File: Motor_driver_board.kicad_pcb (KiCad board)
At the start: 4 copper layers, 90 x 90 mm, 93 parts, among them J1 USB_B_Micro, J2 Screw_Terminal_01x02, J3 Screw_Terminal_01x02, J4 Screw_Terminal_01x03, SW1 Boot, SW2 Reset, U1 LM2596DSADJG, U10 NTMFS5C628NLT1G, U11 NTMFS5C628NLT1G, U12 NTMFS5C628NLT1G, U13 LM393, U2 TPS62A01ADRL, U3 ESP32-S3-MINI-1, U4 USBLC6-2SC6, U5 DRV8323RSRGZR, U6 NTMFS5C628NLT1G, U7 NTMFS5C628NLT1G, U8 NTMFS5C628NLT1G, U9 NTMFS5C628NLT1G

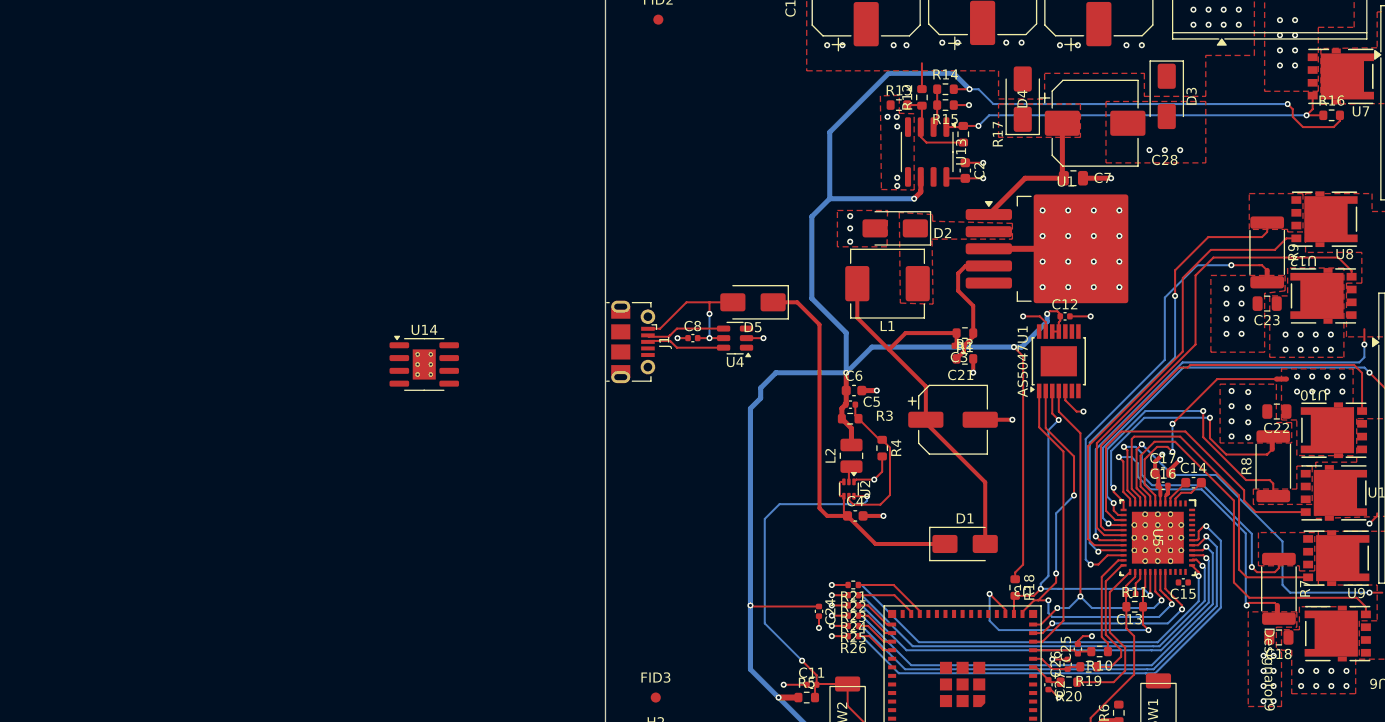
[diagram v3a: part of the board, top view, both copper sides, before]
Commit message: changed regulators, added resistor for slew rate on braking mosfet
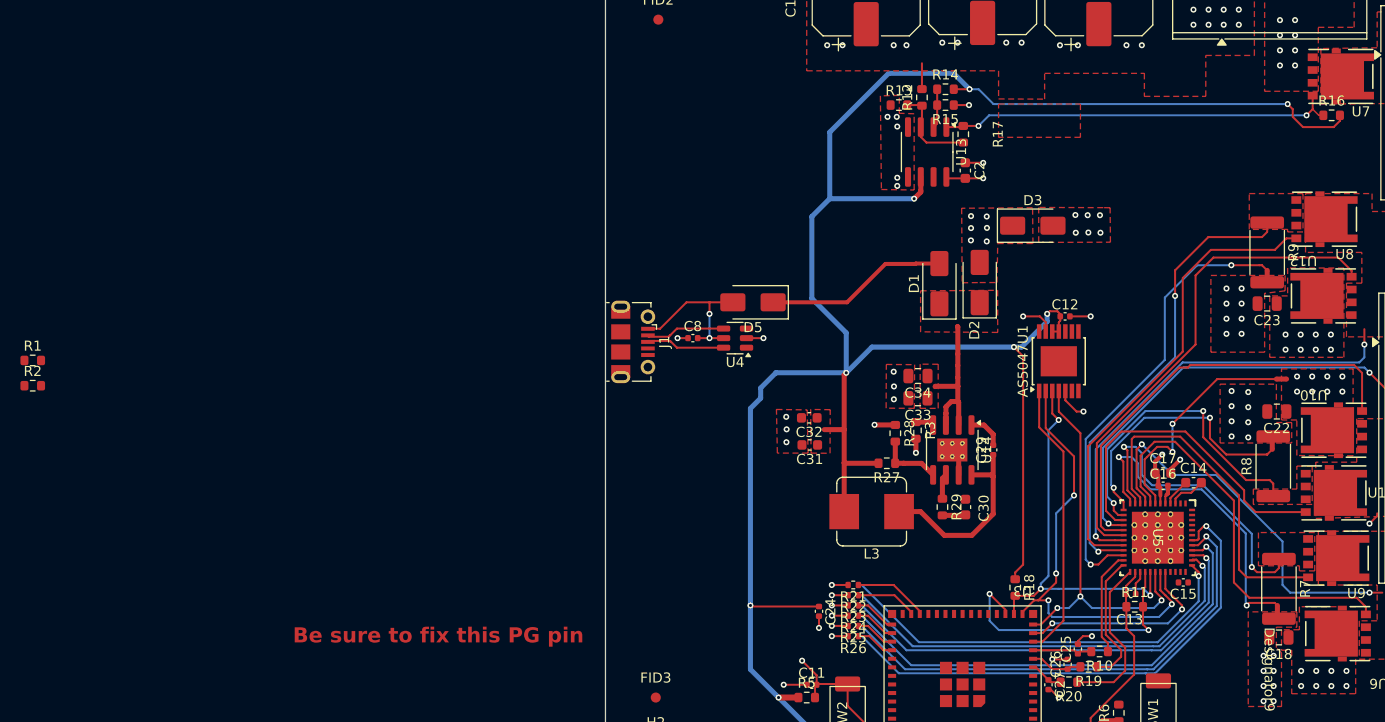
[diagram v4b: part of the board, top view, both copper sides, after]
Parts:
- removed C21: 220 uF, Capacitor_SMD:CP_Elec_6.3x7.7
- removed C28: 100 uF, Capacitor_SMD:CP_Elec_8x10
- removed C3: 15 nF, Capacitor_SMD:C_0402_1005Metric
- removed C4: 4.7 uF, Capacitor_SMD:C_0603_1608Metric
- removed C5: 10 pF, Capacitor_SMD:C_0402_1005Metric
- removed C6: 22 uF, Capacitor_SMD:C_0603_1608Metric
- removed C7: 4.7 uF, Capacitor_SMD:C_0805_2012Metric
- removed D4: SS34, Diode_SMD:D_SMA
- removed L1: 33 uH, Inductor_SMD:L_TechFuse_SL0630
- removed L2: 1.0 uH, Inductor_SMD:L_1008_2520Metric
- removed R4: 100k, Resistor_SMD:R_0603_1608Metric
- removed U1: LM2596DSADJG, Package_TO_SOT_SMD:TO-263-5_TabPin6
- removed U2: TPS62A01ADRL, Package_TO_SOT_SMD:SOT-563
- added C29: 0.1 uF, Capacitor_SMD:C_0402_1005Metric, F.Cu at (167.4, 101.9)
- added C30: 5.6 nF, Capacitor_SMD:C_0603_1608Metric, F.Cu at (164.6, 107.6)
- added C31: 22 uF, Capacitor_SMD:C_0603_1608Metric, F.Cu at (149.2, 101.4)
- added C32: 22 uF, Capacitor_SMD:C_0603_1608Metric, F.Cu at (149.1, 98.7)
- added C33: 10 uF, Capacitor_SMD:C_0805_2012Metric, F.Cu at (159.9, 96.8)
- added C34: 10 uF, Capacitor_SMD:C_0805_2012Metric, F.Cu at (159.9, 94.6)
- added L3: 6.8 uH, Inductor_SMD:L_Bourns_SRP7028A_7.3x6.6mm, F.Cu at (155.3, 108.0)
- added R27: 31.6k, Resistor_SMD:R_0603_1608Metric, F.Cu at (156.8, 103.2)
- added R28: 10k, Resistor_SMD:R_0603_1608Metric, F.Cu at (157.6, 100.2)
- added R29: 9.31k, Resistor_SMD:R_0603_1608Metric, F.Cu at (162.3, 107.6)
- D1, D2: value SS14 -> SS16
- R1: value 3.1k -> 2.2k
- R2: value 1.0k -> 2.2k
- R3: value 470 k -> 200k
- moved R1 92.6 mm to (72.0, 93.0), turned to 0 degrees
- moved R2 92.6 mm to (72.0, 95.5)
- moved U14 53.1 mm to (163.3, 101.9), turned to -90 degrees
- moved D1 26.0 mm to (162.0, 85.4), turned to 90 degrees
- moved D3 18.5 mm to (171.3, 79.6), turned to 0 degrees
- moved D2 9.96 mm to (166.0, 85.3), turned to 90 degrees
- moved R3 6.63 mm to (159.7, 100.0), turned to -90 degrees
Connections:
- D1 pad 1: +5V -> Net-(D1-K)
- D1 pad 2: Net-(D1-A) -> +5V
- D2 pad 1: Net-(D2-K) -> Net-(D1-K)
- D2 pad 2: GND -> +24V
- R1 pad 1: Net-(U1-FEEDBACK) -> unconnected-(R1-Pad1)
- R1 pad 2: Net-(D1-A) -> unconnected-(R1-Pad2)
- R2 pad 1: Net-(U1-FEEDBACK) -> unconnected-(R2-Pad1)
- R2 pad 2: GND -> unconnected-(R2-Pad2)
- R3 pad 1: +3.3V -> Net-(U14-CLK)
- R3 pad 2: Net-(U2-FB) -> GND
- U14 pad 1: unconnected-(U14-BST-Pad1) -> Net-(U14-BST)
- U14 pad 2: unconnected-(U14-Vin-Pad2) -> Net-(D1-K)
- U14 pad 3: unconnected-(U14-EN-Pad3) -> Net-(D1-K)
- U14 pad 4: unconnected-(U14-CLK-Pad4) -> Net-(U14-CLK)
- U14 pad 5: unconnected-(U14-FB-Pad5) -> Net-(U14-FB)
- U14 pad 6: unconnected-(U14-COMP-Pad6) -> Net-(U14-COMP)
- U14 pad 7: unconnected-(U14-GND-Pad7) -> GND
- U14 pad 8: unconnected-(U14-SW-Pad8) -> Net-(U14-SW)
- U14 pad 9: unconnected-(U14-GND-Pad9) -> GND
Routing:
- net Net-(D1-A): track 39.9 -> 0.00 mm
- net /ESP32_S3_mini/PG: track 43.9 -> 15.6 mm, vias 2 -> 1
- net +5V: track 41.9 -> 18.1 mm
- net Net-(U14-SW): track 0.00 -> 19.3 mm
- net GND: track 52.2 -> 33.3 mm, vias 90 -> 76
- net Net-(U2-FB): track 15.6 -> 0.00 mm
- net Net-(D1-K): track 0.00 -> 15.3 mm
- net Net-(D4-K): track 14.5 -> 0.00 mm
- net Net-(U1-FEEDBACK): track 13.1 -> 0.00 mm
- net +3.3V: track 265.0 -> 276.6 mm
- net Net-(U14-FB): track 0.00 -> 6.41 mm
- net Net-(U14-BST): track 0.00 -> 3.61 mm
- net Net-(U14-COMP): track 0.00 -> 2.51 mm
- net Net-(C30-Pad1): track 0.00 -> 2.31 mm
- net Net-(U14-CLK): track 0.00 -> 1.83 mm
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- added copper zone on F.Cu, net (none)
- added copper zone on F.Cu, net +3.3V
- added copper zone on F.Cu, net Net-(D1-K)
- removed copper zone on F.Cu, net Net-(D2-K)
- removed copper zone on F.Cu, net Net-(D4-K)
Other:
- board text added: "Be sure to fix this PG pin"
